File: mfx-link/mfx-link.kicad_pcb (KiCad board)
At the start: 2 copper layers, 50 x 50 mm, 59 parts, among them P1 CONN_01X02, P2 CONN_02X03, P3 CONN_01X02, P4 Grove I2C, P5 IBT-2, P6 CONN_01X02, P7 CONN_01X03, P8 Grove UART, P9 MFX, Q1 BC547, Q2 BC547, Q3 BC547, SW1 SW_PUSH, U1 LM393-1, U2 7805, U3 PIC16F1705, U4 6N137, U5 7805

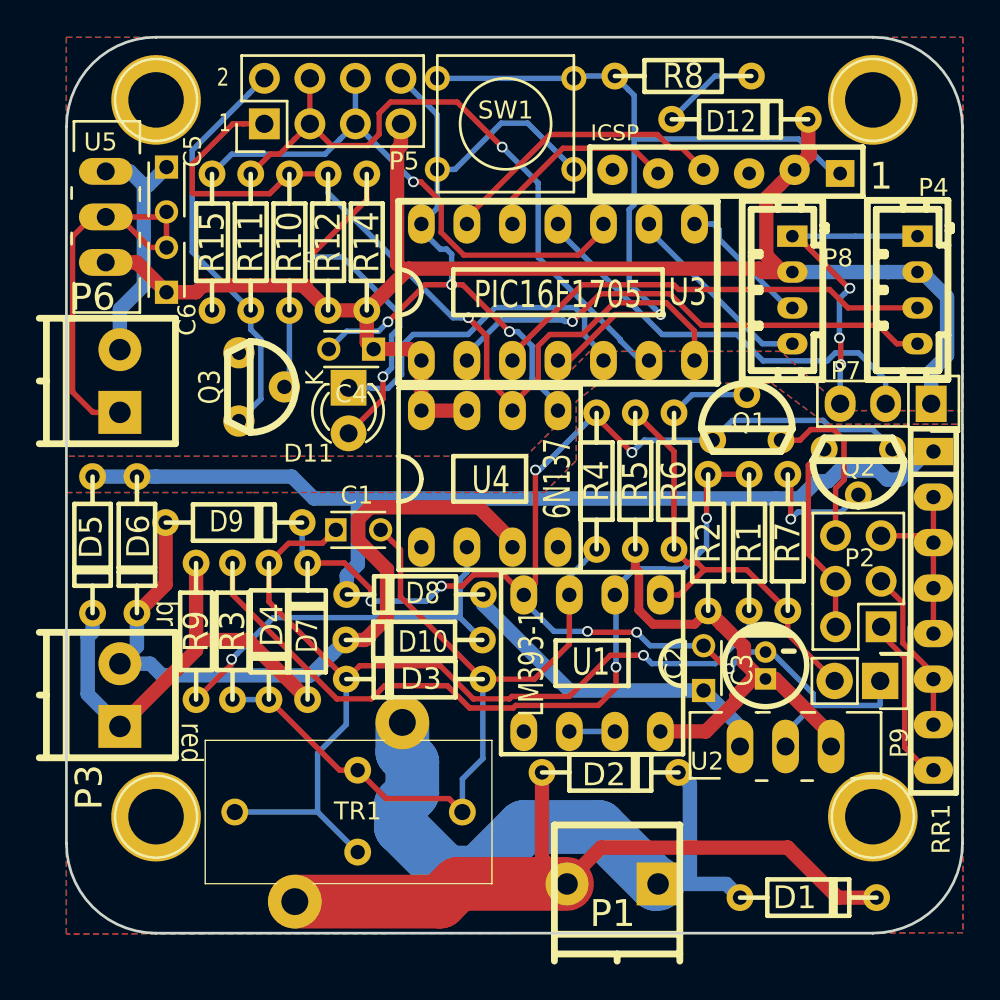
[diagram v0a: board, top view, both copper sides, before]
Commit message: fix diodes
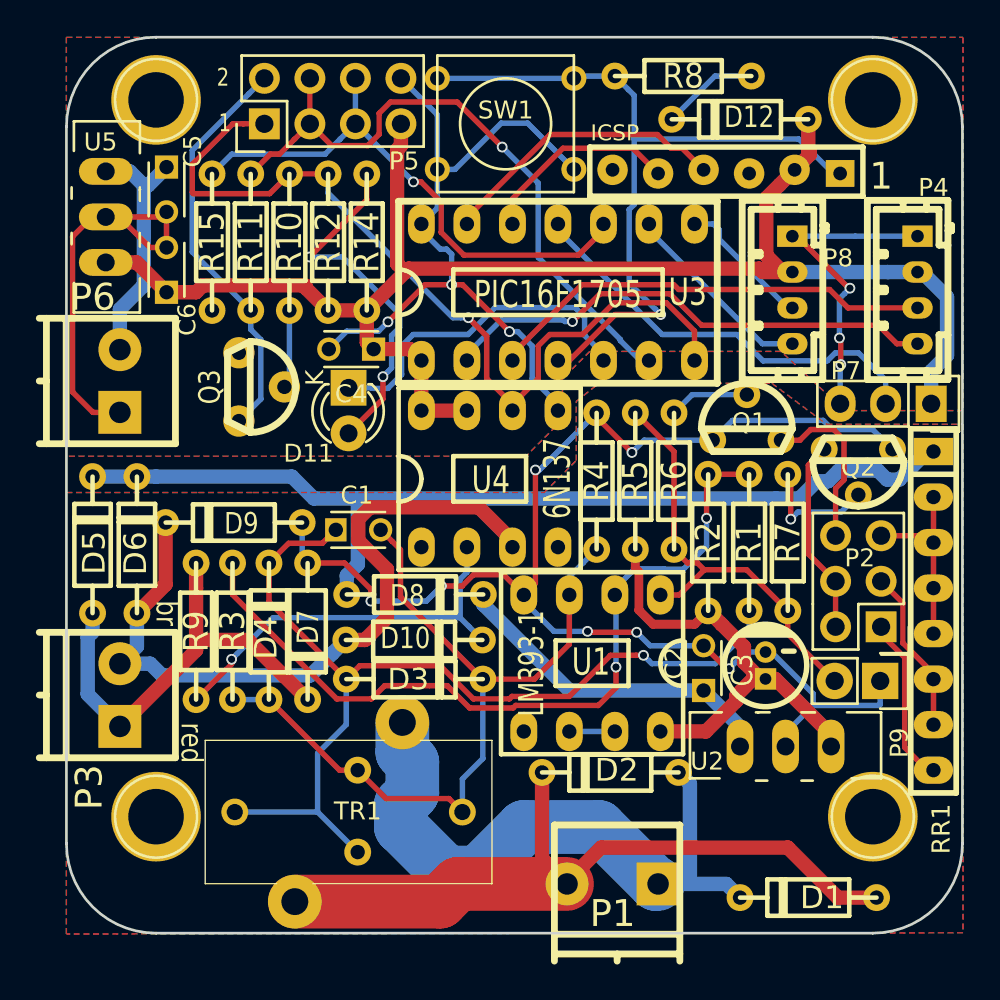
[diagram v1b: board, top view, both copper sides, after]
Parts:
- R12: value 4k7 -> 390
- turned D1 to 180 degrees
- turned D10 to 0 degrees
- turned D12 to 180 degrees
- turned D2 to 180 degrees
- turned D3 to 0 degrees
- turned D4 to 90 degrees
- turned D5 to 90 degrees
- turned D6 to 90 degrees
- turned D7 to 270 degrees
- turned D8 to 0 degrees
- turned D9 to 180 degrees
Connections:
- D1 pad 1: /boost_1 -> /boost_2
- D1 pad 2: /boost_2 -> /boost_1
- D10 pad 1: Net-(D10-Pad1) -> /brown
- D10 pad 2: /brown -> Net-(D10-Pad2)
- D12 pad 1: Net-(D12-Pad1) -> VDD
- D12 pad 2: VDD -> Net-(D12-Pad2)
- D2 pad 1: /boost_2 -> /boost_1
- D2 pad 2: /boost_1 -> /boost_2
- D3 pad 1: Net-(C1-Pad2) -> Net-(C1-Pad1)
- D3 pad 2: Net-(C1-Pad1) -> Net-(C1-Pad2)
- D4 pad 1: Net-(C1-Pad1) -> Net-(C1-Pad2)
- D4 pad 2: Net-(C1-Pad2) -> Net-(C1-Pad1)
- D5 pad 1: Net-(D5-Pad1) -> /red
- D5 pad 2: /red -> Net-(D5-Pad2)
- D6 pad 1: Net-(D5-Pad1) -> /brown
- D6 pad 2: /brown -> Net-(D5-Pad2)
- D7 pad 1: /red -> GND
- D7 pad 2: GND -> /red
- D8 pad 1: /GVI -> Net-(D5-Pad2)
- D8 pad 2: Net-(D5-Pad1) -> /GVI
- D9 pad 1: /brown -> GND
- D9 pad 2: GND -> /brown
- R8 pad 2: Net-(D12-Pad1) -> Net-(D12-Pad2)
- R9 pad 1: Net-(D10-Pad1) -> Net-(D10-Pad2)
- RR1 pad 1: Net-(D5-Pad1) -> Net-(D5-Pad2)
- U4 pad 2: Net-(D10-Pad1) -> Net-(D10-Pad2)
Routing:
- net Net-(D5-Pad2): track 0.00 -> 54.7 mm
- net Net-(D5-Pad1): track 54.7 -> 0.00 mm
- net Net-(D10-Pad2): track 0.00 -> 22.6 mm, vias 0 -> 1
- net Net-(D10-Pad1): track 22.6 -> 0.00 mm, vias 1 -> 0
- net Net-(D12-Pad2): track 0.00 -> 5.44 mm
- net Net-(D12-Pad1): track 5.44 -> 0.00 mm

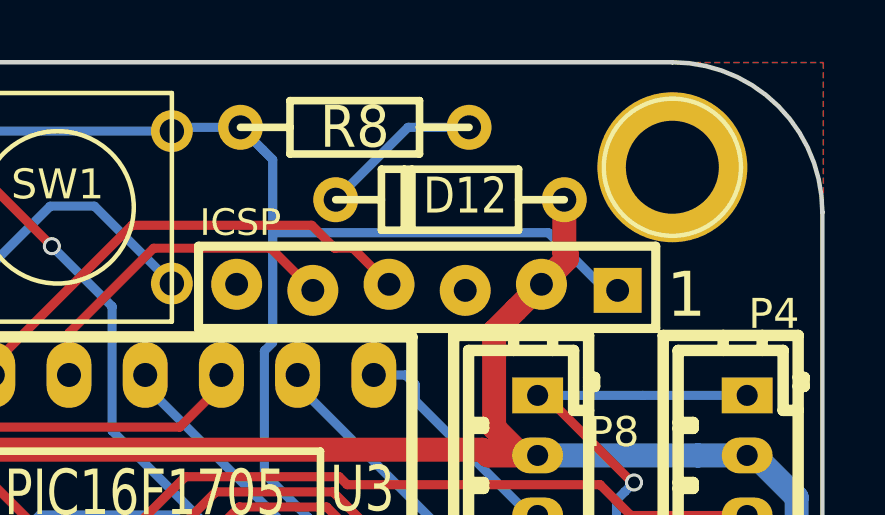
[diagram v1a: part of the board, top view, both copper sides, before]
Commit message: fix diode pins
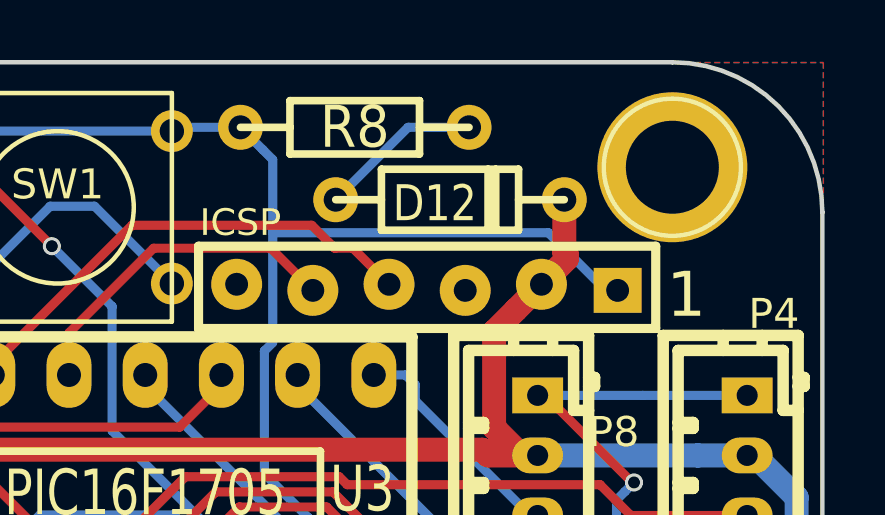
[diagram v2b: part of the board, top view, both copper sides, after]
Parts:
- turned D12 to 0 degrees
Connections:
- D12 pad 1: VDD -> Net-(D12-Pad1)
- D12 pad 2: Net-(D12-Pad2) -> VDD
- R8 pad 2: Net-(D12-Pad2) -> Net-(D12-Pad1)
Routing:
- net Net-(D12-Pad2): track 5.44 -> 0.00 mm
- net Net-(D12-Pad1): track 0.00 -> 5.44 mm
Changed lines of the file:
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@@
     (links 122)
     (no_connects 0)
-    (area 82.000001 67.15 149.6504 132.1752)
+    (area 82.000001 67.15 152.075405 132.1752)
     (thickness 1.6)
     (drawings 15)
@@
     (mod_text_size 1 1)
     (mod_text_width 0.15)
-    (pad_size 1.2 1.3)
-    (pad_drill 0.8)
+    (pad_size 3 1.5)
+    (pad_drill 1.00076)
     (pad_to_mask_clearance 0.2)
     (aux_axis_origin 0 0)
@@
   (net 40 "Net-(D5-Pad2)")
   (net 41 "Net-(D10-Pad2)")
-  (net 42 "Net-(D12-Pad2)")
+  (net 42 "Net-(D12-Pad1)")
   (net_class Default "This is the default net class."
     (clearance 0.2)
@@
     (add_net "Net-(D11-Pad1)")
     (add_net "Net-(D11-Pad2)")
-    (add_net "Net-(D12-Pad2)")
+    (add_net "Net-(D12-Pad1)")
     (add_net "Net-(D5-Pad2)")
     (add_net "Net-(JP1-Pad6)")
@@
     (add_net /red)
     (add_net VDD)
+  )
+  (module w_pth_diodes:diode_do35 (layer F.Cu)
+    (at 96.4565 108.331 90)
+    (descr "Diode, DO-35 package")
+    (fp_text reference D5 (at -0.4445 0.08636 90) (layer F.SilkS)
+      (effects (font (thickness 0.3048)))
+    )
+    (fp_text value 1N4007 (at 0 -2.54 90) (layer F.SilkS) hide
+      (effects (font (thickness 0.3048)))
+    )
+    (fp_line (start 1.524 1.016) (end 1.524 -1.016) (layer F.SilkS) (width 0.254))
+    (fp_line (start 1.27 -1.016) (end 1.27 1.016) (layer F.SilkS) (width 0.254))
+    (fp_line (start 3.81 0) (end 2.286 0) (layer F.SilkS) (width 0.254))
+    (fp_line (start -2.286 0) (end -3.81 0) (layer F.SilkS) (width 0.254))
+    (fp_line (start -2.286 -1.016) (end 2.286 -1.016) (layer F.SilkS) (width 0.254))
+    (fp_line (start 2.286 -1.016) (end 2.286 1.016) (layer F.SilkS) (width 0.254))
+    (fp_line (start 2.286 1.016) (end -2.286 1.016) (layer F.SilkS) (width 0.254))
+    (fp_line (start -2.286 1.016) (end -2.286 -1.016) (layer F.SilkS) (width 0.254))
+    (pad 1 thru_hole circle (at -3.81 0 90) (size 1.5 1.5) (drill 0.8) (layers *.Cu *.Mask F.SilkS)
+      (net 22 /red))
+    (pad 2 thru_hole circle (at 3.81 0 90) (size 1.5 1.5) (drill 0.8) (layers *.Cu *.Mask F.SilkS)
+      (net 40 "Net-(D5-Pad2)"))
+    (model walter/pth_diodes/diode_do35.wrl
+      (at (xyz 0 0 0))
+      (scale (xyz 1 1 1))
+      (rotate (xyz 0 0 0))
+    )
   )
   (module w_pth_circuits:dil_8-300_socket (layer F.Cu)
@@
   )
   (module w_pth_diodes:diode_do35 (layer F.Cu)
-    (at 96.4565 108.331 90)
-    (descr "Diode, DO-35 package")
-    (fp_text reference D5 (at -0.4445 0.08636 90) (layer F.SilkS)
-      (effects (font (thickness 0.3048)))
-    )
-    (fp_text value 1N4007 (at 0 -2.54 90) (layer F.SilkS) hide
-      (effects (font (thickness 0.3048)))
-    )
-    (fp_line (start 1.524 1.016) (end 1.524 -1.016) (layer F.SilkS) (width 0.254))
-    (fp_line (start 1.27 -1.016) (end 1.27 1.016) (layer F.SilkS) (width 0.254))
-    (fp_line (start 3.81 0) (end 2.286 0) (layer F.SilkS) (width 0.254))
-    (fp_line (start -2.286 0) (end -3.81 0) (layer F.SilkS) (width 0.254))
-    (fp_line (start -2.286 -1.016) (end 2.286 -1.016) (layer F.SilkS) (width 0.254))
-    (fp_line (start 2.286 -1.016) (end 2.286 1.016) (layer F.SilkS) (width 0.254))
-    (fp_line (start 2.286 1.016) (end -2.286 1.016) (layer F.SilkS) (width 0.254))
-    (fp_line (start -2.286 1.016) (end -2.286 -1.016) (layer F.SilkS) (width 0.254))
-    (pad 1 thru_hole circle (at -3.81 0 90) (size 1.5 1.5) (drill 0.8) (layers *.Cu *.Mask F.SilkS)
-      (net 22 /red))
-    (pad 2 thru_hole circle (at 3.81 0 90) (size 1.5 1.5) (drill 0.8) (layers *.Cu *.Mask F.SilkS)
-      (net 40 "Net-(D5-Pad2)"))
-    (model walter/pth_diodes/diode_do35.wrl
-      (at (xyz 0 0 0))
-      (scale (xyz 1 1 1))
-      (rotate (xyz 0 0 0))
-    )
-  )
-  (module w_pth_diodes:diode_do35 (layer F.Cu)
     (at 98.933 108.331 90)
     (descr "Diode, DO-35 package")
@@
       (net 26 /MCLR))
     (pad 2 thru_hole circle (at 3.81 0) (size 1.5 1.5) (drill 0.8) (layers *.Cu *.Mask F.SilkS)
-      (net 42 "Net-(D12-Pad2)"))
+      (net 42 "Net-(D12-Pad1)"))
     (model walter/pth_resistors/rc03.wrl
       (at (xyz 0 0 0))
@@
   )
   (module w_pth_diodes:diode_do35 (layer F.Cu)
-    (at 132.588 84.582 180)
+    (at 132.588 84.582)
     (descr "Diode, DO-35 package")
-    (fp_text reference D12 (at -0.508 0.127 180) (layer F.SilkS)
+    (fp_text reference D12 (at -0.508 0.127) (layer F.SilkS)
       (effects (font (size 1.2 1) (thickness 0.25)))
     )
-    (fp_text value BAT43 (at 16.7005 0.9525 180) (layer F.SilkS) hide
+    (fp_text value BAT43 (at 16.7005 0.9525) (layer F.SilkS) hide
       (effects (font (size 1.2 1) (thickness 0.25)))
     )
@@
     (fp_line (start 2.286 1.016) (end -2.286 1.016) (layer F.SilkS) (width 0.254))
     (fp_line (start -2.286 1.016) (end -2.286 -1.016) (layer F.SilkS) (width 0.254))
-    (pad 1 thru_hole circle (at -3.81 0 180) (size 1.5 1.5) (drill 0.8) (layers *.Cu *.Mask F.SilkS)
+    (pad 1 thru_hole circle (at -3.81 0) (size 1.5 1.5) (drill 0.8) (layers *.Cu *.Mask F.SilkS)
+      (net 42 "Net-(D12-Pad1)"))
+    (pad 2 thru_hole circle (at 3.81 0) (size 1.5 1.5) (drill 0.8) (layers *.Cu *.Mask F.SilkS)
       (net 13 VDD))
-    (pad 2 thru_hole circle (at 3.81 0 180) (size 1.5 1.5) (drill 0.8) (layers *.Cu *.Mask F.SilkS)
-      (net 42 "Net-(D12-Pad2)"))
     (model walter/pth_diodes/diode_do35.wrl
       (at (xyz 0 0 0))

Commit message: fix it - now !
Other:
- board text added: "mfx-Link V1.1"
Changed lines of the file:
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@@
     (links 122)
     (no_connects 0)
-    (area 82.000001 67.15 152.075405 132.1752)
+    (area 91.9925 75.15 155 132.1752)
     (thickness 1.6)
-    (drawings 15)
+    (drawings 16)
     (tracks 551)
     (zones 0)
@@
       (effects (font (size 1 1) (thickness 0.15)))
     )
-    (fp_text value 100nF (at 1.25 2.5) (layer F.Fab)
+    (fp_text value 100nF (at 1.2827 0.0127) (layer F.Fab)
       (effects (font (size 1 1) (thickness 0.15)))
     )
@@
     )
   )
+  (dimension 50 (width 0.3) (layer Dwgs.User)
+    (gr_text "50,000 mm" (at 148.35 105 90) (layer Dwgs.User)
+      (effects (font (size 1.5 1.5) (thickness 0.3)))
+    )
+    (feature1 (pts (xy 145 80) (xy 149.7 80)))
+    (feature2 (pts (xy 145 130) (xy 149.7 130)))
+    (crossbar (pts (xy 147 130) (xy 147 80)))
+    (arrow1a (pts (xy 147 80) (xy 147.586421 81.126504)))
+    (arrow1b (pts (xy 147 80) (xy 146.413579 81.126504)))
+    (arrow2a (pts (xy 147 130) (xy 147.586421 128.873496)))
+    (arrow2b (pts (xy 147 130) (xy 146.413579 128.873496)))
+  )
+  (dimension 50 (width 0.3) (layer Dwgs.User)
+    (gr_text "50,000 mm" (at 120 76.65) (layer Dwgs.User)
+      (effects (font (size 1.5 1.5) (thickness 0.3)))
+    )
+    (feature1 (pts (xy 145 80) (xy 145 75.3)))
+    (feature2 (pts (xy 95 80) (xy 95 75.3)))
+    (crossbar (pts (xy 95 78) (xy 145 78)))
+    (arrow1a (pts (xy 145 78) (xy 143.873496 78.586421)))
+    (arrow1b (pts (xy 145 78) (xy 143.873496 77.413579)))
+    (arrow2a (pts (xy 95 78) (xy 96.126504 78.586421)))
+    (arrow2b (pts (xy 95 78) (xy 96.126504 77.413579)))
+  )
+  (gr_text "mfx-Link\nV1.1" (at 99.187 127.8255) (layer F.SilkS)
+    (effects (font (size 1.2 1) (thickness 0.2)))
+  )
   (gr_text 1 (at 103.8352 84.7852) (layer F.SilkS)
     (effects (font (size 1 0.8) (thickness 0.2)))
@@
     (effects (font (size 1.5 1.5) (thickness 0.3)))
   )
-  (dimension 50 (width 0.3) (layer Dwgs.User)
-    (gr_text "50,000 mm" (at 88.65 105 270) (layer Dwgs.User)
-      (effects (font (size 1.5 1.5) (thickness 0.3)))
-    )
-    (feature1 (pts (xy 100 130) (xy 87.3 130)))
-    (feature2 (pts (xy 100 80) (xy 87.3 80)))
-    (crossbar (pts (xy 90 80) (xy 90 130)))
-    (arrow1a (pts (xy 90 130) (xy 89.413579 128.873496)))
-    (arrow1b (pts (xy 90 130) (xy 90.586421 128.873496)))
-    (arrow2a (pts (xy 90 80) (xy 89.413579 81.126504)))
-    (arrow2b (pts (xy 90 80) (xy 90.586421 81.126504)))
-  )
-  (dimension 50 (width 0.3) (layer Dwgs.User)
-    (gr_text "50,000 mm" (at 120 68.65) (layer Dwgs.User)
-      (effects (font (size 1.5 1.5) (thickness 0.3)))
-    )
-    (feature1 (pts (xy 145 85) (xy 145 67.3)))
-    (feature2 (pts (xy 95 85) (xy 95 67.3)))
-    (crossbar (pts (xy 95 70) (xy 145 70)))
-    (arrow1a (pts (xy 145 70) (xy 143.873496 70.586421)))
-    (arrow1b (pts (xy 145 70) (xy 143.873496 69.413579)))
-    (arrow2a (pts (xy 95 70) (xy 96.126504 70.586421)))
-    (arrow2b (pts (xy 95 70) (xy 96.126504 69.413579)))
-  )
   (gr_arc (start 100 85) (end 95 85) (angle 90) (layer Edge.Cuts) (width 0.15))

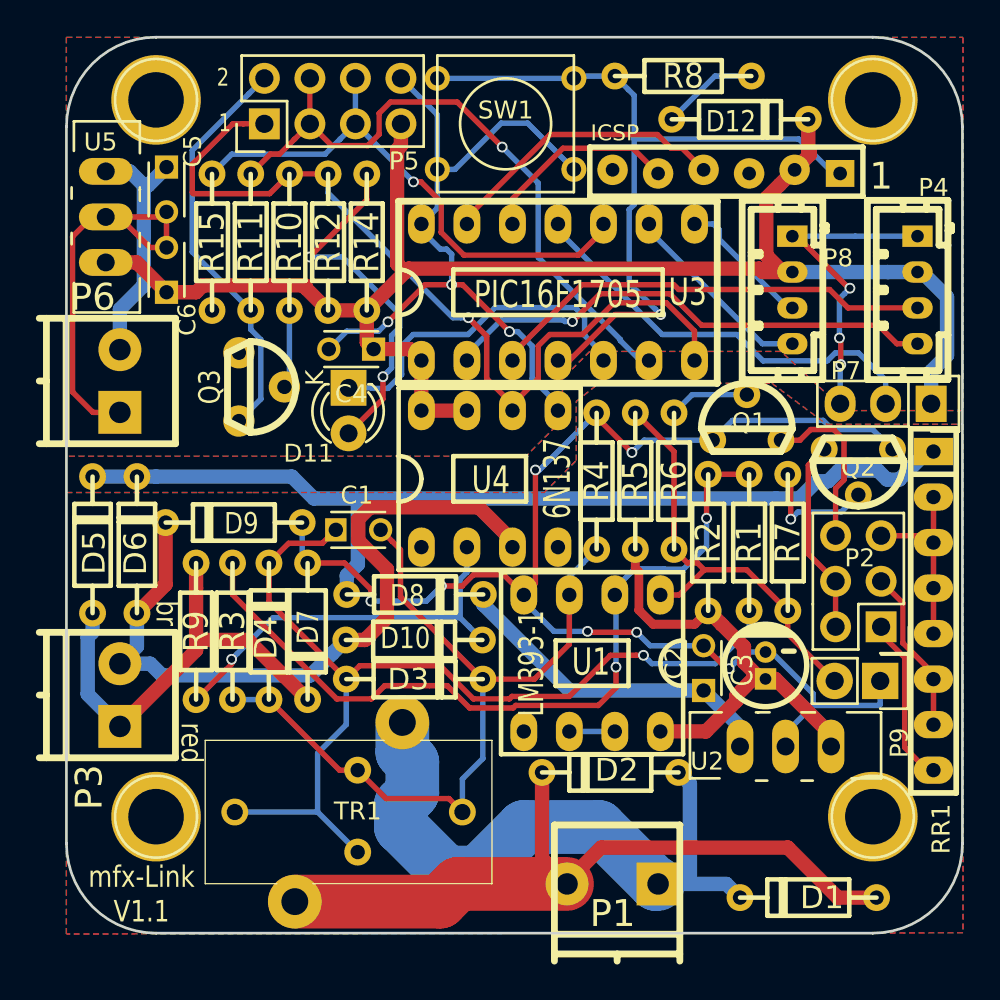
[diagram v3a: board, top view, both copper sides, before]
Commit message: fix BC547 pinning
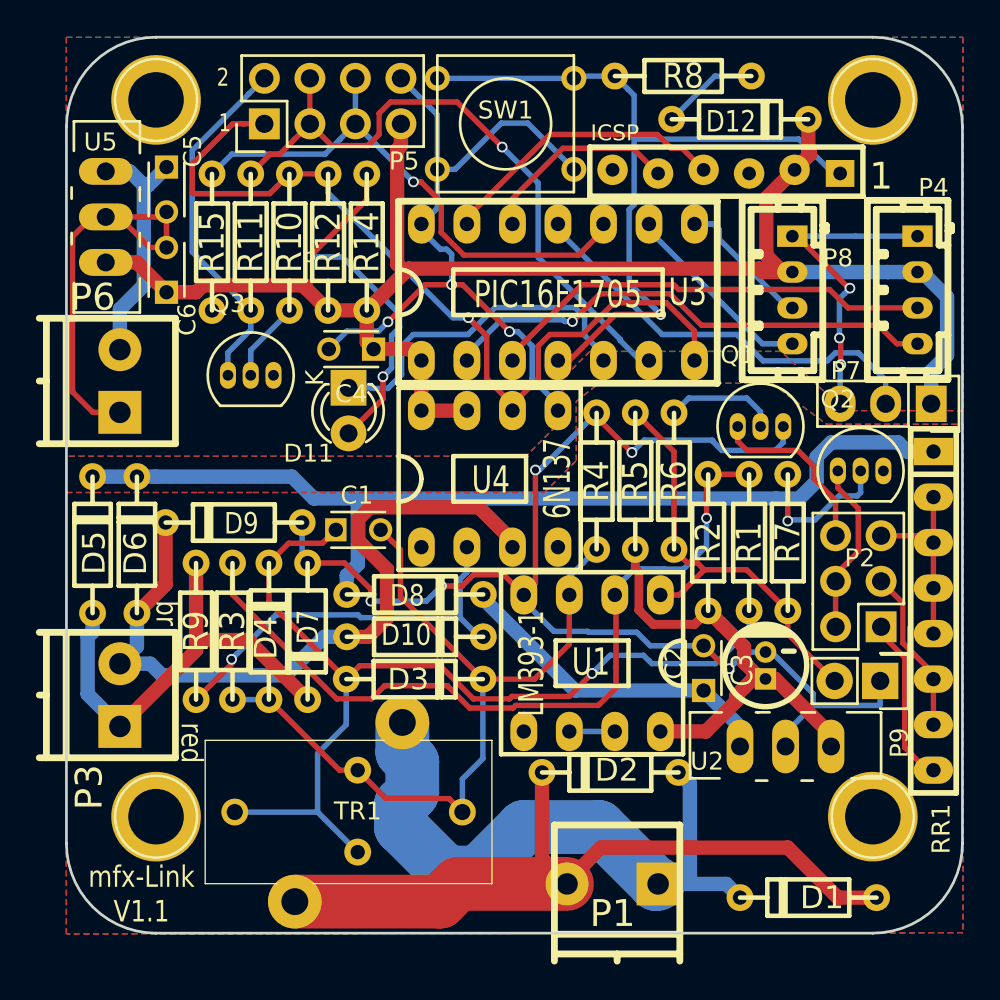
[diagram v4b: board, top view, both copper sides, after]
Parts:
- Q1, Q2, Q3: footprint w_to:to92_3 -> TO_SOT_Packages_THT:TO-92_Inline_Narrow_Oval
- moved Q3 1.40 mm to (104.0, 98.9), turned to 0 degrees
- moved Q2 1.28 mm to (138.0, 104.2), turned to 0 degrees
- moved Q1 0.52 mm to (132.5, 101.7)
- moved D10 0.18 mm to (114.5, 113.5)
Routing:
- net GND: track 75.8 -> 69.9 mm, vias 7 -> 5
- net Net-(P5-Pad2): track 22.9 -> 20.1 mm
- net Net-(Q2-Pad2): track 6.91 -> 8.77 mm
- net Net-(Q1-Pad2): track 4.48 -> 6.31 mm
- net Net-(P2-Pad2): track 10.9 -> 9.70 mm
- net Net-(D5-Pad2): track 54.7 -> 55.5 mm
- net Net-(P2-Pad6): track 9.55 -> 10.3 mm
- net Net-(R1-Pad1): vias 2 -> 1

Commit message: optimize routing
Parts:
- moved D7 0.25 mm to (108.7, 113.2)
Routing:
- net GND: track 69.9 -> 83.1 mm, vias 5 -> 8
- net Net-(R1-Pad1): track 44.9 -> 40.1 mm, vias 1 -> 2
- net Net-(C1-Pad2): track 45.6 -> 44.0 mm
- net Net-(C1-Pad1): track 55.2 -> 56.3 mm
- net Net-(P9-Pad2): track 24.3 -> 23.7 mm
- net Net-(D10-Pad2): vias 1 -> 0
